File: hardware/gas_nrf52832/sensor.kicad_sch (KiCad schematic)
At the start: 43 parts, among them IC1 REF1112AIDBZR, IC3 LPV821DBVR, IC4 LPV821DBVR, IC5 LPV821DBVR, U3 MMBFJ177, U5 BME680

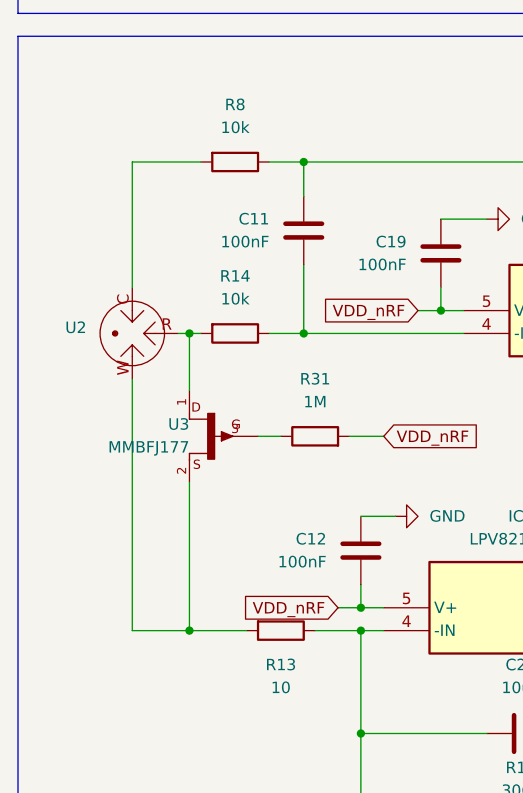
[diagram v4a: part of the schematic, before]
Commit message: feat: hw revision 2.0.1
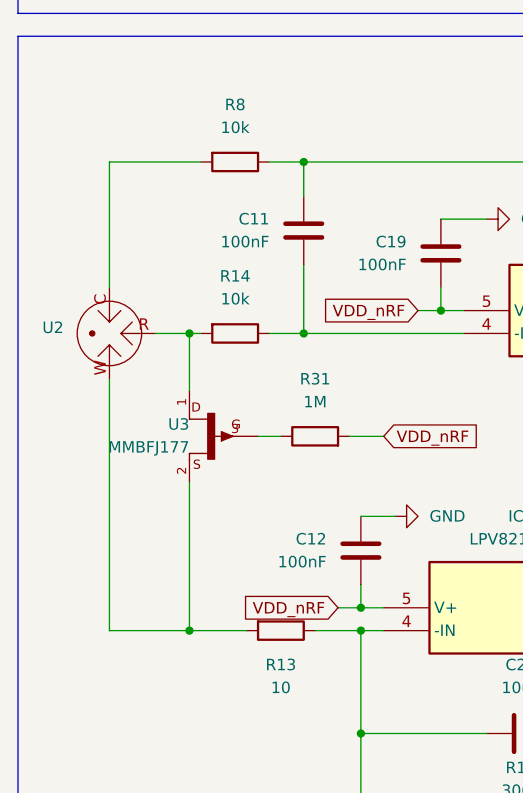
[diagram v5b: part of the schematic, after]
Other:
- moved on the sheet: U2
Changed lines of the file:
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@@
 	(wire
 		(pts
-			(xy 33.02 128.27) (xy 34.29 128.27)
+			(xy 30.48 128.27) (xy 34.29 128.27)
 		)
 		(stroke
@@
 	(wire
 		(pts
-			(xy 27.94 109.22) (xy 27.94 123.19)
+			(xy 25.4 109.22) (xy 25.4 123.19)
 		)
 		(stroke
@@
 	(wire
 		(pts
-			(xy 27.94 161.29) (xy 34.29 161.29)
+			(xy 25.4 161.29) (xy 34.29 161.29)
 		)
 		(stroke
@@
 	(wire
 		(pts
-			(xy 27.94 109.22) (xy 35.56 109.22)
+			(xy 25.4 109.22) (xy 35.56 109.22)
 		)
 		(stroke
@@
 	(wire
 		(pts
-			(xy 27.94 133.35) (xy 27.94 161.29)
+			(xy 25.4 133.35) (xy 25.4 161.29)
 		)
 		(stroke
@@
 		(on_board yes)
 		(dnp no)
-		(fields_autoplaced yes)
 		(property "Reference" "R25"
 			(at 254 46.9899 0)
@@
 	(symbol
 		(lib_id "ss2198_h2s:ss2198_h2s")
-		(at 27.94 128.27 180)
+		(at 25.4 128.27 180)
 		(unit 1)
 		(exclude_from_sim no)
@@
 		(fields_autoplaced yes)
 		(property "Reference" "U2"
-			(at 22.86 127.6349 0)
+			(at 20.32 127.6349 0)
 			(effects
 				(font
@@
 		)
 		(property "Value" "~"
-			(at 22.86 129.54 0)
+			(at 20.32 129.54 0)
 			(effects
 				(font
@@
 		)
 		(property "Footprint" "HHS:SS2198_H2S"
-			(at 27.94 128.27 0)
+			(at 25.4 128.27 0)
 			(effects
 				(font
@@
 		)
 		(property "Datasheet" ""
-			(at 27.94 128.27 0)
+			(at 25.4 128.27 0)
 			(effects
 				(font
@@
 		)
 		(property "Description" ""
-			(at 27.94 128.27 0)
+			(at 25.4 128.27 0)
 			(effects
 				(font
@@
 		)
 		(property "Type" ""
-			(at 27.94 128.27 0)
+			(at 25.4 128.27 0)
 			(effects
 				(font
